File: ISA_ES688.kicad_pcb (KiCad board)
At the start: 4 copper layers, 104.1 x 99.1 mm, 114 parts, among them J1 ISA BUS, J2 Interrupt Select, J3 Address Select, J4 DMA Select, J5 Joystick/MIDI, J6 LINE OUT, J7 MIC, J8 LINE IN, J9 SPKR OUT, U1 74LS14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

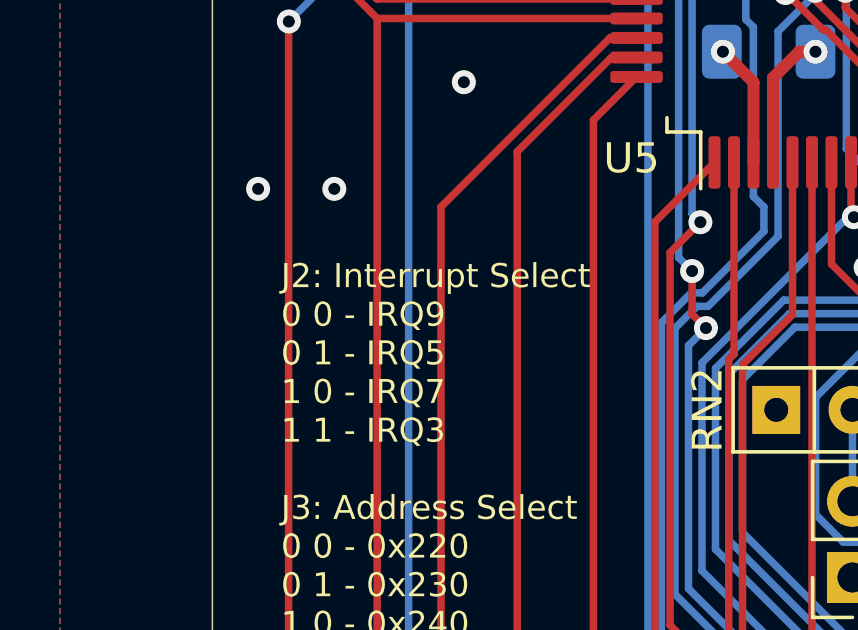
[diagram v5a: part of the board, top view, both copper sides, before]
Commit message: Changed silkscreen for IRQ
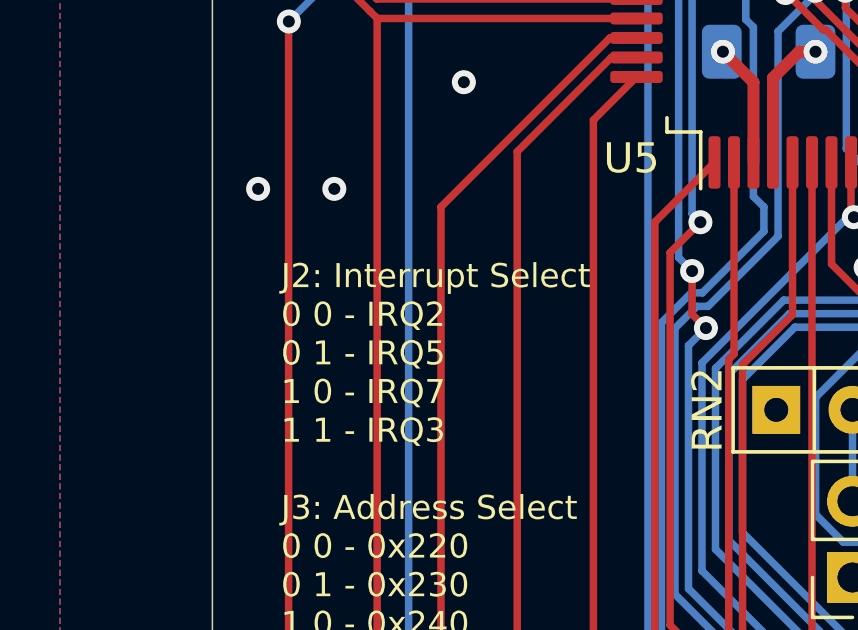
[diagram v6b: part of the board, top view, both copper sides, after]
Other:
- board text added: "J2: Interrupt Select 0 0 - IRQ2 0 1 - IRQ5 1 0 - IRQ7 1 1 - IRQ3 J3: Address Select 0 0 - 0x220 0 1 - 0x230 1 0 - 0x240 1 1 - 0x250 J4: DMA Select 0 0 - None 0 1 - DMA2 1 0 - DMA1 1 1 - DMA3"
- board text removed: "J2: Interrupt Select 0 0 - IRQ9 0 1 - IRQ5 1 0 - IRQ7 1 1 - IRQ3 J3: Address Select 0 0 - 0x220 0 1 - 0x230 1 0 - 0x240 1 1 - 0x250 J4: DMA Select 0 0 - None 0 1 - DMA2 1 0 - DMA1 1 1 - DMA3"
